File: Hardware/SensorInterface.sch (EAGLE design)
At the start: 73 parts, among them J3 CONN_32.54_SCREW, J4 CONN_32.54_SCREW, J5 CONN_42.54_SCREW, Q1 DMG3404, Q2 DMG3404, Q3 DMG3404, Q4 DMG3404, Q5 DMG3404, U10 SN74AHC1G86DCK, U11 MCP6041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

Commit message: Layout cleanup ready for review
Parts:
- removed U4: (no value), bschulz:SN74LVC1G14DCK
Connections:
- net 3V3: no longer U4G2.P$V+
- net GND: no longer U4G2.P$V-
- net VREF: now also U14.PA0

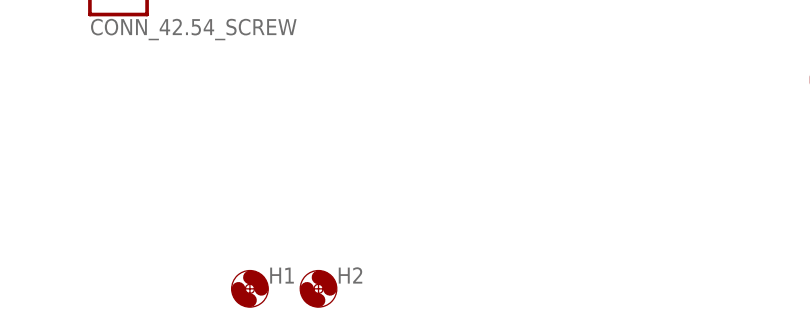
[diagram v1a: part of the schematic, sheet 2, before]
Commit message: SE corner hole added
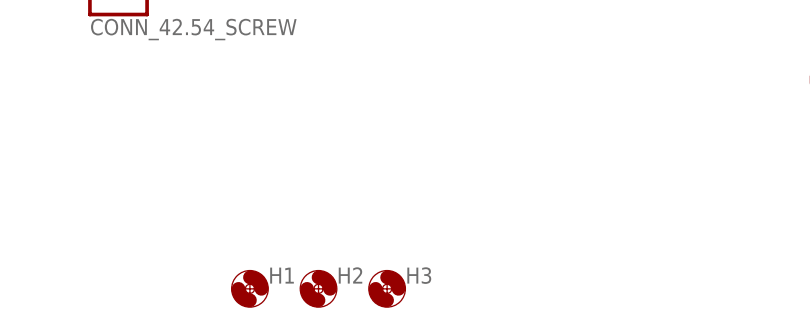
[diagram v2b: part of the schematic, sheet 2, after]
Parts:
- added H3: (no value), bschulz:MOUNTING_HOLE2_NP
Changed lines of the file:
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@@
 <?xml version="1.0" encoding="utf-8"?>
 <!DOCTYPE eagle SYSTEM "eagle.dtd">
-<eagle version="9.2.1">
+<eagle version="9.2.2">
 <drawing>
 <settings>
@@
 <part name="H1" library="bschulz" deviceset="MOUNTING_HOLE" device="2_NP"/>
 <part name="H2" library="bschulz" deviceset="MOUNTING_HOLE" device="2_NP"/>
+<part name="H3" library="bschulz" deviceset="MOUNTING_HOLE" device="2_NP"/>
 </parts>
 <sheets>
@@
 <attribute name="VALUE" x="121.412" y="17.8562" size="1.778" layer="96"/>
 </instance>
+<instance part="H3" gate="G$1" x="127" y="20.32" smashed="yes">
+<attribute name="NAME" x="129.032" y="20.9042" size="1.778" layer="95"/>
+<attribute name="VALUE" x="129.032" y="17.8562" size="1.778" layer="96"/>
+</instance>
 </instances>

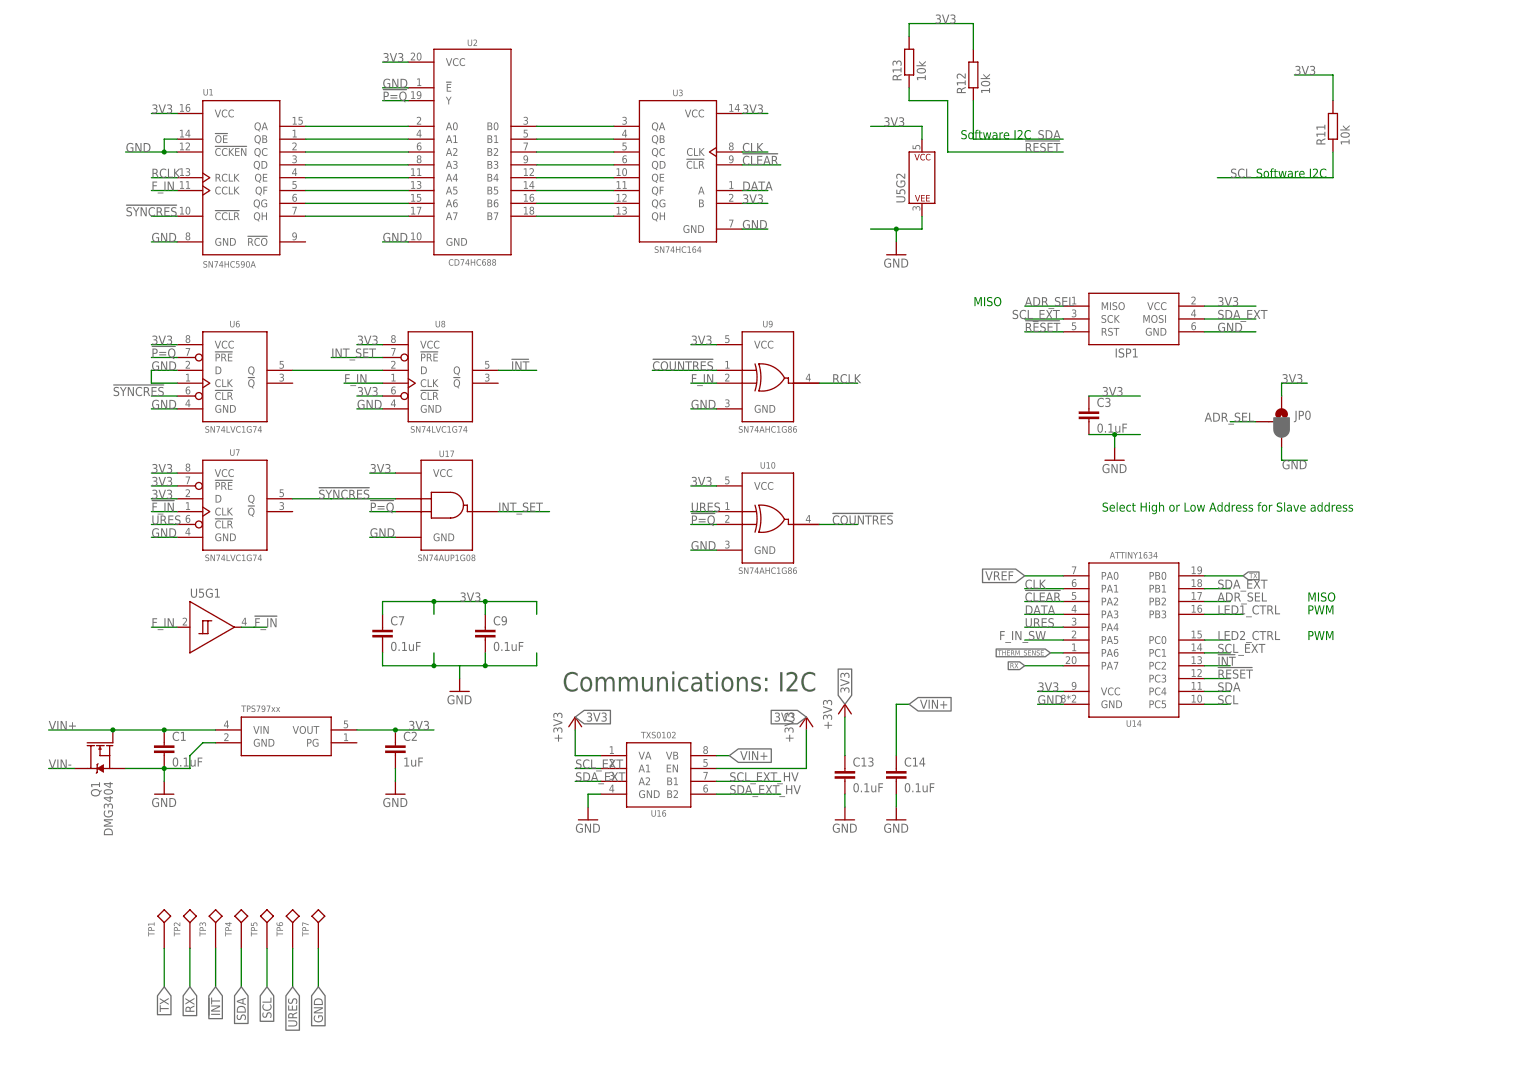
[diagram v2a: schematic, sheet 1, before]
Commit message: Added PDFs and replaced OSHW logo
Added PDFs for board (clean) and schematic (nearly clean), also replaced the OSHW logo with one from ColdSilicon which uses the correct layer
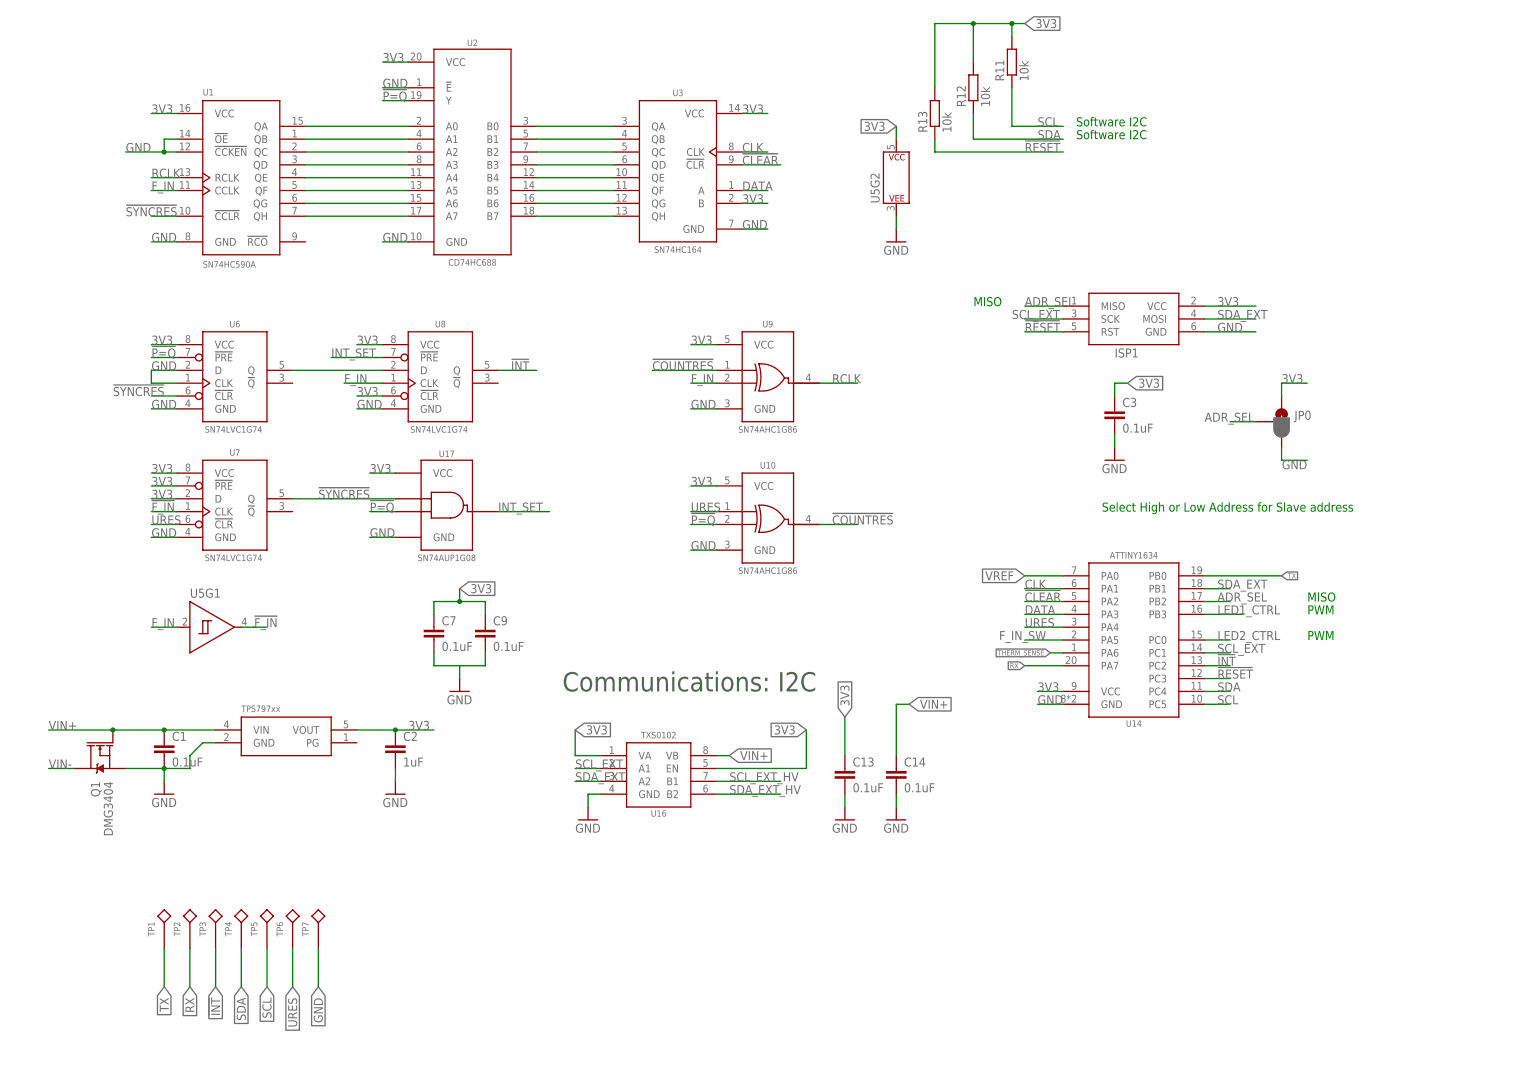
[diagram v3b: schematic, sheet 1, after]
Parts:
- LOGO1: device SparkFun-Aesthetics:OSHW-LOGOM -> bschulz:OSHW-LOGOM
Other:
- note removed: "Switch FETs to DMG3404?"
- moved on the sheet: C11, C12, C15, C3, C7, R11, R12, R13, U5G2

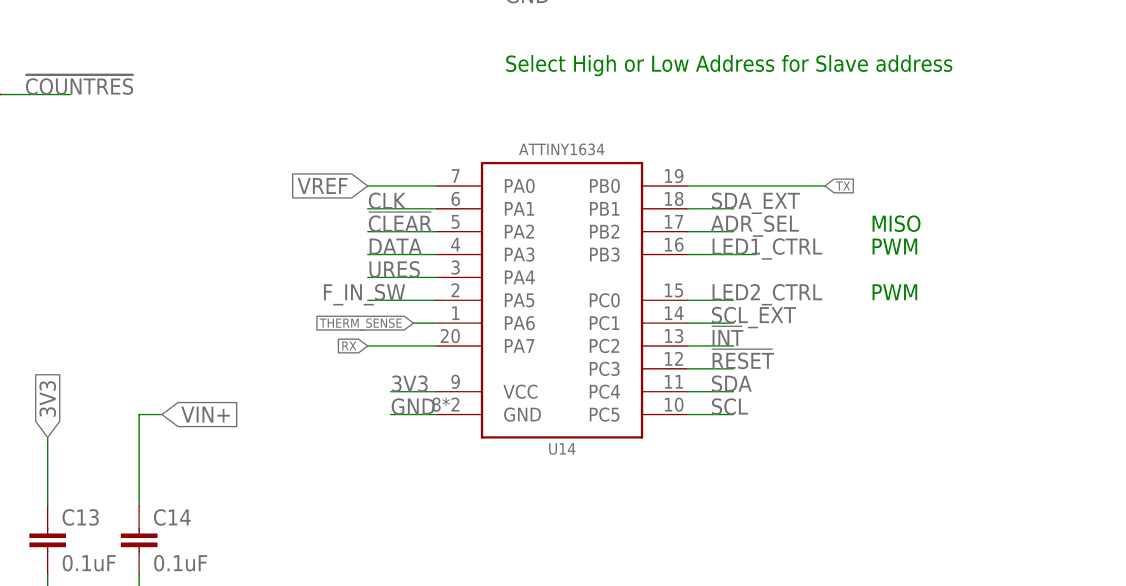
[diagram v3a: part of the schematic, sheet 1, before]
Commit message: Added preliminary driver interface
Added in progress Calypso firmware driver, also added additional labeling to schematic for sensor interface
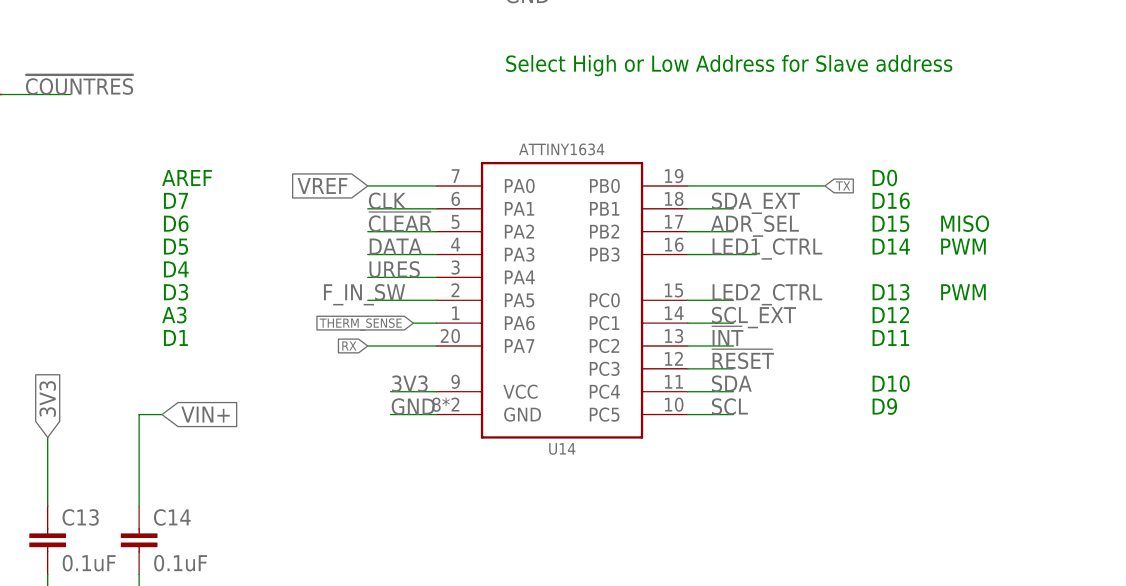
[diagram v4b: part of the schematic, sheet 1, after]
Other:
- note added: "A3"
- note added: "AREF"
- note added: "D0"
- note added: "D1"
- note added: "D10"
- note added: "D11"
- note added: "D12"
- note added: "D13"
- note added: "D14"
- note added: "D15"
- note added: "D16"
- note added: "D3"
- note added: "D4"
- note added: "D5"
- note added: "D6"
- note added: "D7"
- note added: "D9"
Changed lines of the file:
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@@
 <text x="223.52" y="111.76" size="1.778" layer="91" ratio="15">Select High or Low Address for Slave address</text>
 <text x="116.84" y="76.2" size="3.81" layer="97">Communications: I2C</text>
-<text x="264.16" y="91.44" size="1.778" layer="91">PWM</text>
-<text x="264.16" y="86.36" size="1.778" layer="91">PWM</text>
-<text x="264.16" y="93.98" size="1.778" layer="91">MISO</text>
+<text x="271.78" y="91.44" size="1.778" layer="91">PWM</text>
+<text x="271.78" y="86.36" size="1.778" layer="91">PWM</text>
+<text x="271.78" y="93.98" size="1.778" layer="91">MISO</text>
 <text x="198.12" y="152.4" size="1.778" layer="91">MISO</text>
+<text x="185.42" y="99.06" size="1.778" layer="91">AREF</text>
+<text x="185.42" y="96.52" size="1.778" layer="91">D7</text>
+<text x="185.42" y="93.98" size="1.778" layer="91">D6</text>
+<text x="185.42" y="91.44" size="1.778" layer="91">D5</text>
+<text x="185.42" y="88.9" size="1.778" layer="91">D4</text>
+<text x="185.42" y="86.36" size="1.778" layer="91">D3</text>
+<text x="185.42" y="83.82" size="1.778" layer="91">A3</text>
+<text x="185.42" y="81.28" size="1.778" layer="91">D1</text>
+<text x="264.16" y="99.06" size="1.778" layer="91">D0</text>
+<text x="264.16" y="96.52" size="1.778" layer="91">D16</text>
+<text x="264.16" y="93.98" size="1.778" layer="91">D15</text>
+<text x="264.16" y="91.44" size="1.778" layer="91">D14</text>
+<text x="264.16" y="86.36" size="1.778" layer="91">D13</text>
+<text x="264.16" y="83.82" size="1.778" layer="91">D12</text>
+<text x="264.16" y="81.28" size="1.778" layer="91">D11</text>
+<text x="264.16" y="76.2" size="1.778" layer="91">D10</text>
+<text x="264.16" y="73.66" size="1.778" layer="91">D9</text>
 </plain>
 <instances>

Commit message: Cleaned up schematic for report
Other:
- note added: "Control Logic"
- note added: "Counter"
- note added: "DAC and Analog"
- note added: "External Connectors"
- note added: "Input Select"
- note added: "LED Current Constant Current Drive"
- note added: "Microcontroller"
- note added: "Power"
- moved on the sheet: C1, C11, C12, C13, C14, C15, C16, C17, C2, C3, C4, C5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
